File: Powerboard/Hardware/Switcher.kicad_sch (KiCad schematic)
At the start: 40 parts, among them J1 Conn_01x03_MountingPin, J2 XT60PW-F, J7 XT60PW-M, J8 Conn_01x04_Male, U2 ESP32-S3, Y1 40MHz±10ppm

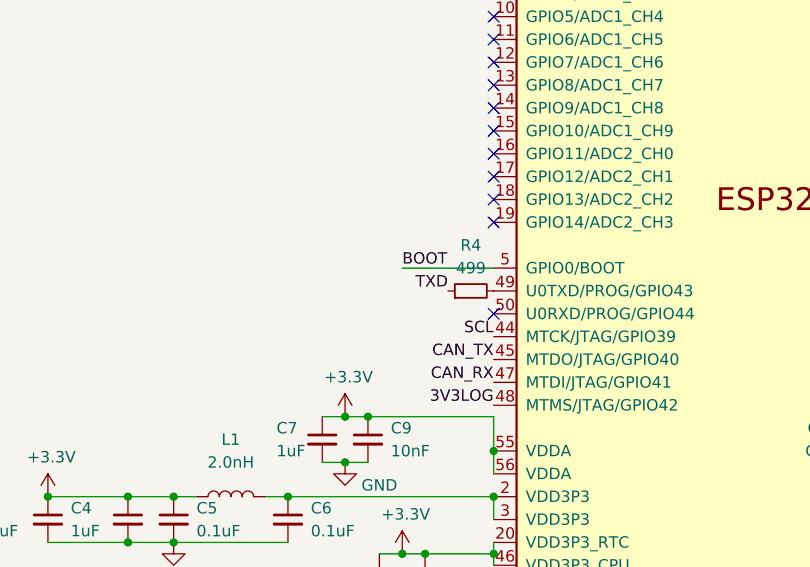
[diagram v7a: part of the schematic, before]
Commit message: rxd/txd testpoints
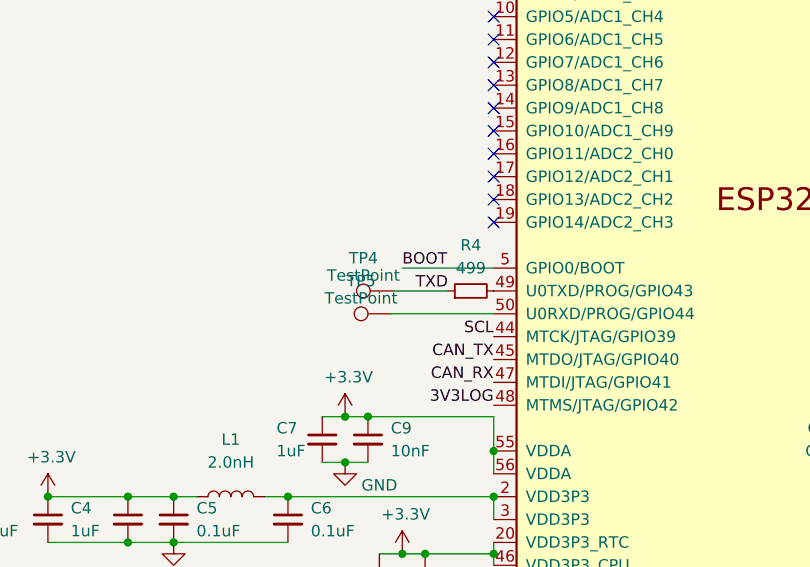
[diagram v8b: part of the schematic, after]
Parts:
- added TP4, TP5: TestPoint, TestPoint:TestPoint_Pad_D1.0mm, symbol Connector:TestPoint
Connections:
- net TXD: now also TP4.1
- net at U2.50 (U0RXD/PROG/GPIO44): now also TP5.1
- no-connect marks 32 -> 31
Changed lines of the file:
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@@
   (no_connect (at 242.062 90.932))
   (no_connect (at 176.022 73.152))
-  (no_connect (at 176.022 116.332))
   (no_connect (at 242.062 123.952))
   (wire (pts (xy 129.032 170.942) (xy 122.682 170.942))
@@
     (stroke (width 0) (type default))
   )
+  (wire (pts (xy 164.846 113.792) (xy 170.942 113.792))
+    (stroke (width 0) (type default))
+  )
   (wire (pts (xy 165.862 62.992) (xy 169.672 62.992))
     (stroke (width 0) (type default))
@@
   )
   (wire (pts (xy 262.382 127.762) (xy 262.382 129.032))
+    (stroke (width 0) (type default))
+  )
+  (wire (pts (xy 164.592 116.332) (xy 176.022 116.332))
     (stroke (width 0) (type default))
   )
@@
         )
       )
+    )
+  )
+  (symbol (lib_id "Connector:TestPoint") (at 164.592 116.332 90) (unit 1)
+    (in_bom yes) (on_board yes) (dnp no) (fields_autoplaced)
+    (property "Reference" "TP5" (at 161.29 112.6871 90)
+      (effects (font (size 1.27 1.27)))
+    )
+    (property "Value" "TestPoint" (at 161.29 114.6081 90)
+      (effects (font (size 1.27 1.27)))
+    )
+    (property "Footprint" "TestPoint:TestPoint_Pad_D1.0mm" (at 164.592 111.252 0)
+      (effects (font (size 1.27 1.27)) hide)
+    )
+    (property "Datasheet" "~" (at 164.592 111.252 0)
+      (effects (font (size 1.27 1.27)) hide)
+    )
+    (pin "1")
+    (instances
+      (project "Switcher"
+        (path "/e63e39d7-6ac0-4ffd-8aa3-1841a4541b55"
+          (reference "TP5") (unit 1)
+        )
+      )
+    )
+  )
+  (symbol (lib_id "Connector:TestPoint") (at 164.846 113.792 90) (unit 1)
+    (in_bom yes) (on_board yes) (dnp no) (fields_autoplaced)
+    (property "Reference" "TP4" (at 161.544 110.1471 90)
+      (effects (font (size 1.27 1.27)))
+    )
+    (property "Value" "TestPoint" (at 161.544 112.0681 90)
+      (effects (font (size 1.27 1.27)))
+    )
+    (property "Footprint" "TestPoint:TestPoint_Pad_D1.0mm" (at 164.846 108.712 0)
+      (effects (font (size 1.27 1.27)) hide)
+    )
+    (property "Datasheet" "~" (at 164.846 108.712 0)
+      (effects (font (size 1.27 1.27)) hide)
+    )
+    (pin "1")
+    (instances
+      (project "Switcher"
+        (path "/e63e39d7-6ac0-4ffd-8aa3-1841a4541b55"
+          (reference "TP4") (unit 1)
+        )
+      )
